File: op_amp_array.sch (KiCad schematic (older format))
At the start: 20 parts

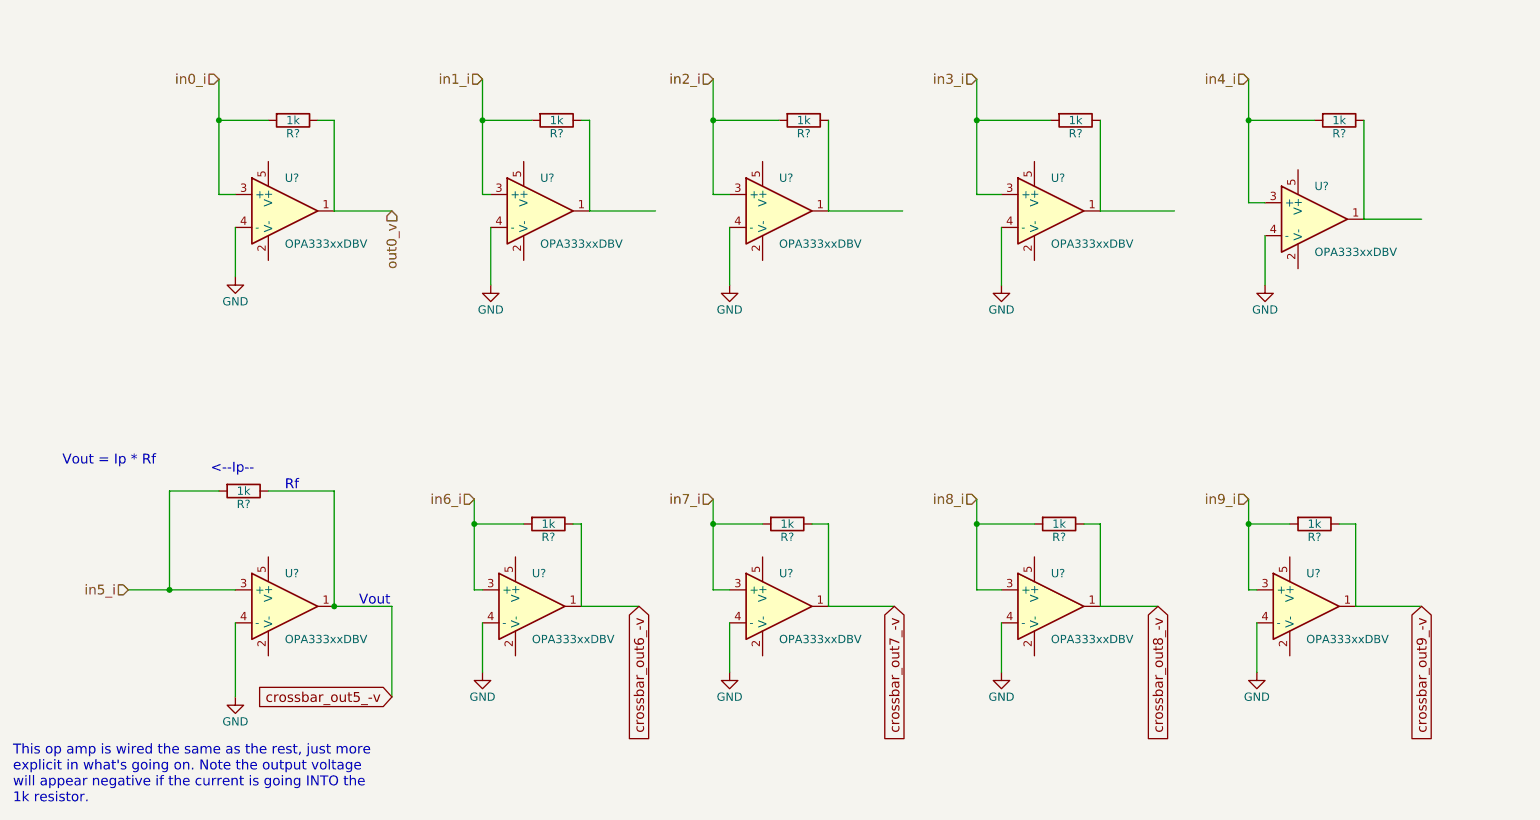
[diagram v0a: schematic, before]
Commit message: Additional Heirarchy Changes
Added resistor pages, still need to update values on them. See weight matrix file.
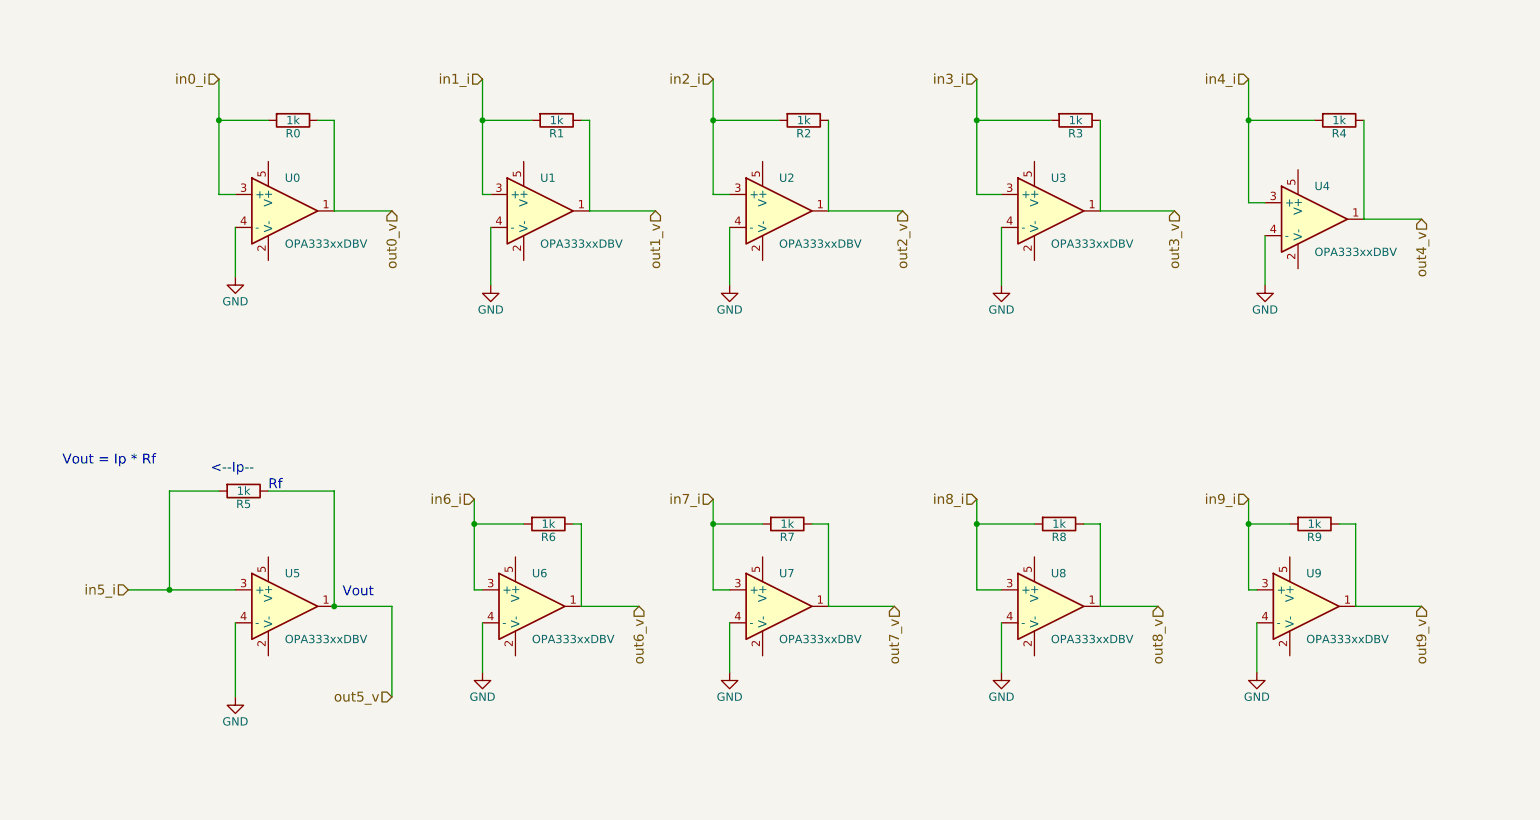
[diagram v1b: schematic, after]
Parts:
- gave numbers to parts that had none: 20
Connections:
- net labels added: out1_v, out2_v, out3_v, out4_v, out5_v, out6_v, out7_v, out8_v, out9_v
- net labels removed: crossbar_out5_-v, crossbar_out6_-v, crossbar_out7_-v, crossbar_out8_-v, crossbar_out9_-v
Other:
- note removed: "This op amp is wired the same as the rest, just more\nexplicit in what's going on. Note the output voltage \nwill appear negative if the current is going INTO the \n1k resistor."
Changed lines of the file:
@@
 $Descr A4 11693 8268
 encoding utf-8
-Sheet 2 3
-Title ""
+Sheet 2 7
+Title "Op Amp Array"
 Date ""
 Rev ""
-Comp ""
+Comp "Emulating NN with Resistor Network"
 Comment1 ""
 Comment2 ""
@@
 $EndDescr
 $Comp
-L OPA333xxDBV U?
+L OPA333xxDBV U4
 U 1 1 5C6B8B0D
 P 8800 2350
-F 0 "U?" H 8800 2550 50  0000 L CNN
+F 0 "U4" H 8800 2550 50  0000 L CNN
 F 1 "OPA333xxDBV" H 8800 2150 50  0000 L CNN
 F 2 "" H 8800 2350 50  0001 C CNN
@@
 $EndComp
 $Comp
-L OPA333xxDBV U?
+L OPA333xxDBV U5
 U 1 1 5C6B8B14
 P 2550 4700
-F 0 "U?" H 2550 4900 50  0000 L CNN
+F 0 "U5" H 2550 4900 50  0000 L CNN
 F 1 "OPA333xxDBV" H 2550 4500 50  0000 L CNN
 F 2 "" H 2550 4700 50  0001 C CNN
@@
 $EndComp
 $Comp
-L OPA333xxDBV U?
+L OPA333xxDBV U7
 U 1 1 5C6B8B1B
 P 5550 4700
-F 0 "U?" H 5550 4900 50  0000 L CNN
+F 0 "U7" H 5550 4900 50  0000 L CNN
 F 1 "OPA333xxDBV" H 5550 4500 50  0000 L CNN
 F 2 "" H 5550 4700 50  0001 C CNN
@@
 $EndComp
 $Comp
-L OPA333xxDBV U?
+L OPA333xxDBV U9
 U 1 1 5C6B8B22
 P 8750 4700
-F 0 "U?" H 8750 4900 50  0000 L CNN
+F 0 "U9" H 8750 4900 50  0000 L CNN
 F 1 "OPA333xxDBV" H 8750 4500 50  0000 L CNN
 F 2 "" H 8750 4700 50  0001 C CNN
@@
 $EndComp
 $Comp
-L OPA333xxDBV U?
+L OPA333xxDBV U2
 U 1 1 5C6B8B29
 P 5550 2300
-F 0 "U?" H 5550 2500 50  0000 L CNN
+F 0 "U2" H 5550 2500 50  0000 L CNN
 F 1 "OPA333xxDBV" H 5550 2100 50  0000 L CNN
 F 2 "" H 5550 2300 50  0001 C CNN
@@
 $EndComp
 $Comp
-L OPA333xxDBV U?
+L OPA333xxDBV U3
 U 1 1 5C6B8B30
 P 7200 2300
-F 0 "U?" H 7200 2500 50  0000 L CNN
+F 0 "U3" H 7200 2500 50  0000 L CNN
 F 1 "OPA333xxDBV" H 7200 2100 50  0000 L CNN
 F 2 "" H 7200 2300 50  0001 C CNN
@@
 $EndComp
 $Comp
-L OPA333xxDBV U?
+L OPA333xxDBV U6
 U 1 1 5C6B8B37
 P 4050 4700
-F 0 "U?" H 4050 4900 50  0000 L CNN
+F 0 "U6" H 4050 4900 50  0000 L CNN
 F 1 "OPA333xxDBV" H 4050 4500 50  0000 L CNN
 F 2 "" H 4050 4700 50  0001 C CNN
@@
 $EndComp
 $Comp
-L OPA333xxDBV U?
+L OPA333xxDBV U8
 U 1 1 5C6B8B3E
 P 7200 4700
-F 0 "U?" H 7200 4900 50  0000 L CNN
+F 0 "U8" H 7200 4900 50  0000 L CNN
 F 1 "OPA333xxDBV" H 7200 4500 50  0000 L CNN
 F 2 "" H 7200 4700 50  0001 C CNN
@@
 $EndComp
 $Comp
-L OPA333xxDBV U?
+L OPA333xxDBV U1
 U 1 1 5C6B8B45
 P 4100 2300
-F 0 "U?" H 4100 2500 50  0000 L CNN
+F 0 "U1" H 4100 2500 50  0000 L CNN
 F 1 "OPA333xxDBV" H 4100 2100 50  0000 L CNN
 F 2 "" H 4100 2300 50  0001 C CNN
@@
 $EndComp
 $Comp
-L OPA333xxDBV U?
+L OPA333xxDBV U0
 U 1 1 5C6B8B4C
 P 2550 2300
-F 0 "U?" H 2550 2500 50  0000 L CNN
+F 0 "U0" H 2550 2500 50  0000 L CNN
 F 1 "OPA333xxDBV" H 2550 2100 50  0000 L CNN
 F 2 "" H 2550 2300 50  0001 C CNN
@@
 	2250 4800 2250 5250
 $Comp
-L R R?
+L R R5
 U 1 1 5C6B8B54
 P 2300 4000
-F 0 "R?" V 2380 4000 50  0000 C CNN
+F 0 "R5" V 2380 4000 50  0000 C CNN
 F 1 "1k" V 2300 4000 50  0000 C CNN
 F 2 "" V 2230 4000 50  0001 C CNN
@@
 	3200 4700 3200 5250
 Connection ~ 2850 4700
-Text GLabel 3200 5250 0    60   Input ~ 0
-crossbar_out5_-v
 Text Notes 1200 3850 0    60   ~ 0
 Vout = Ip * Rf
-Text Notes 3000 4700 0    60   ~ 0
+Text Notes 2900 4650 0    60   ~ 0
 Vout
-Text Notes 2550 4000 0    60   ~ 0
+Text Notes 2450 4000 0    60   ~ 0
 Rf
 Text Notes 2100 3900 0    60   ~ 0
@@
 	8400 2250 8500 2250
 $Comp
-L R R?
+L R R0
 U 1 1 5C6B8B79
 P 2600 1750
-F 0 "R?" V 2680 1750 50  0000 C CNN
+F 0 "R0" V 2680 1750 50  0000 C CNN
 F 1 "1k" V 2600 1750 50  0000 C CNN
 F 2 "" V 2530 1750 50  0001 C CNN
@@
 $EndComp
 $Comp
-L R R?
+L R R1
 U 1 1 5C6B8B80
 P 4200 1750
-F 0 "R?" V 4280 1750 50  0000 C CNN
+F 0 "R1" V 4280 1750 50  0000 C CNN
 F 1 "1k" V 4200 1750 50  0000 C CNN
 F 2 "" V 4130 1750 50  0001 C CNN
@@
 $EndComp
 $Comp
-L R R?
+L R R2
 U 1 1 5C6B8B87
 P 5700 1750
-F 0 "R?" V 5780 1750 50  0000 C CNN
+F 0 "R2" V 5780 1750 50  0000 C CNN
 F 1 "1k" V 5700 1750 50  0000 C CNN
 F 2 "" V 5630 1750 50  0001 C CNN
@@
 $EndComp
 $Comp
-L R R?
+L R R3
 U 1 1 5C6B8B8E
 P 7350 1750
-F 0 "R?" V 7430 1750 50  0000 C CNN
+F 0 "R3" V 7430 1750 50  0000 C CNN
 F 1 "1k" V 7350 1750 50  0000 C CNN
 F 2 "" V 7280 1750 50  0001 C CNN
@@
 $EndComp
 $Comp
-L R R?
+L R R4
 U 1 1 5C6B8B95
 P 8950 1750
-F 0 "R?" V 9030 1750 50  0000 C CNN
+F 0 "R4" V 9030 1750 50  0000 C CNN
 F 1 "1k" V 8950 1750 50  0000 C CNN
 F 2 "" V 8880 1750 50  0001 C CNN
@@
 	8400 4600 8450 4600
 $Comp
-L R R?
+L R R8
 U 1 1 5C6B8BB5
 P 7250 4200
-F 0 "R?" V 7330 4200 50  0000 C CNN
+F 0 "R8" V 7330 4200 50  0000 C CNN
 F 1 "1k" V 7250 4200 50  0000 C CNN
 F 2 "" V 7180 4200 50  0001 C CNN
@@
 $EndComp
 $Comp
-L R R?
+L R R7
 U 1 1 5C6B8BBC
 P 5600 4200
-F 0 "R?" V 5680 4200 50  0000 C CNN
+F 0 "R7" V 5680 4200 50  0000 C CNN
 F 1 "1k" V 5600 4200 50  0000 C CNN
 F 2 "" V 5530 4200 50  0001 C CNN
@@
 $EndComp
 $Comp
-L R R?
+L R R6
 U 1 1 5C6B8BC3
 P 4150 4200
-F 0 "R?" V 4230 4200 50  0000 C CNN
+F 0 "R6" V 4230 4200 50  0000 C CNN
 F 1 "1k" V 4150 4200 50  0000 C CNN
 F 2 "" V 4080 4200 50  0001 C CNN
@@
 $EndComp
 $Comp
-L R R?
+L R R9
 U 1 1 5C6B8BCA
 P 8800 4200
-F 0 "R?" V 8880 4200 50  0000 C CNN
+F 0 "R9" V 8880 4200 50  0000 C CNN
 F 1 "1k" V 8800 4200 50  0000 C CNN
 F 2 "" V 8730 4200 50  0001 C CNN
@@
 Wire Wire Line
 	5850 4200 5850 4700
-Text Notes 900  5900 0    60   ~ 0
-This op amp is wired the same as the rest, just more\nexplicit in what's going on. Note the output voltage \nwill appear negative if the current is going INTO the \n1k resistor.
 $Comp
 L GND #PWR?
@@
 Wire Wire Line
 	3750 4800 3750 5100
-Text GLabel 4700 4700 3    60   Input ~ 0
-crossbar_out6_-v
-Text GLabel 6250 4700 3    60   Input ~ 0
-crossbar_out7_-v
-Text GLabel 7850 4700 3    60   Input ~ 0
-crossbar_out8_-v
-Text GLabel 9450 4700 3    60   Input ~ 0
-crossbar_out9_-v
 Wire Wire Line
 	9050 4700 9450 4700
@@
 Text HLabel 3200 2300 3    60   Input ~ 0
 out0_v
+Text HLabel 4800 2300 3    60   Input ~ 0
+out1_v
+Text HLabel 6300 2300 3    60   Input ~ 0
+out2_v
+Text HLabel 7950 2300 3    60   Input ~ 0
+out3_v
+Text HLabel 9450 2350 3    60   Input ~ 0
+out4_v
+Text HLabel 3200 5250 0    60   Input ~ 0
+out5_v
+Text HLabel 4700 4700 3    60   Input ~ 0
+out6_v
+Text HLabel 6250 4700 3    60   Input ~ 0
+out7_v
+Text HLabel 7850 4700 3    60   Input ~ 0
+out8_v
+Text HLabel 9450 4700 3    60   Input ~ 0
+out9_v
 $EndSCHEMATC

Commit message: Added footprints, finished schematic, began PCB layout
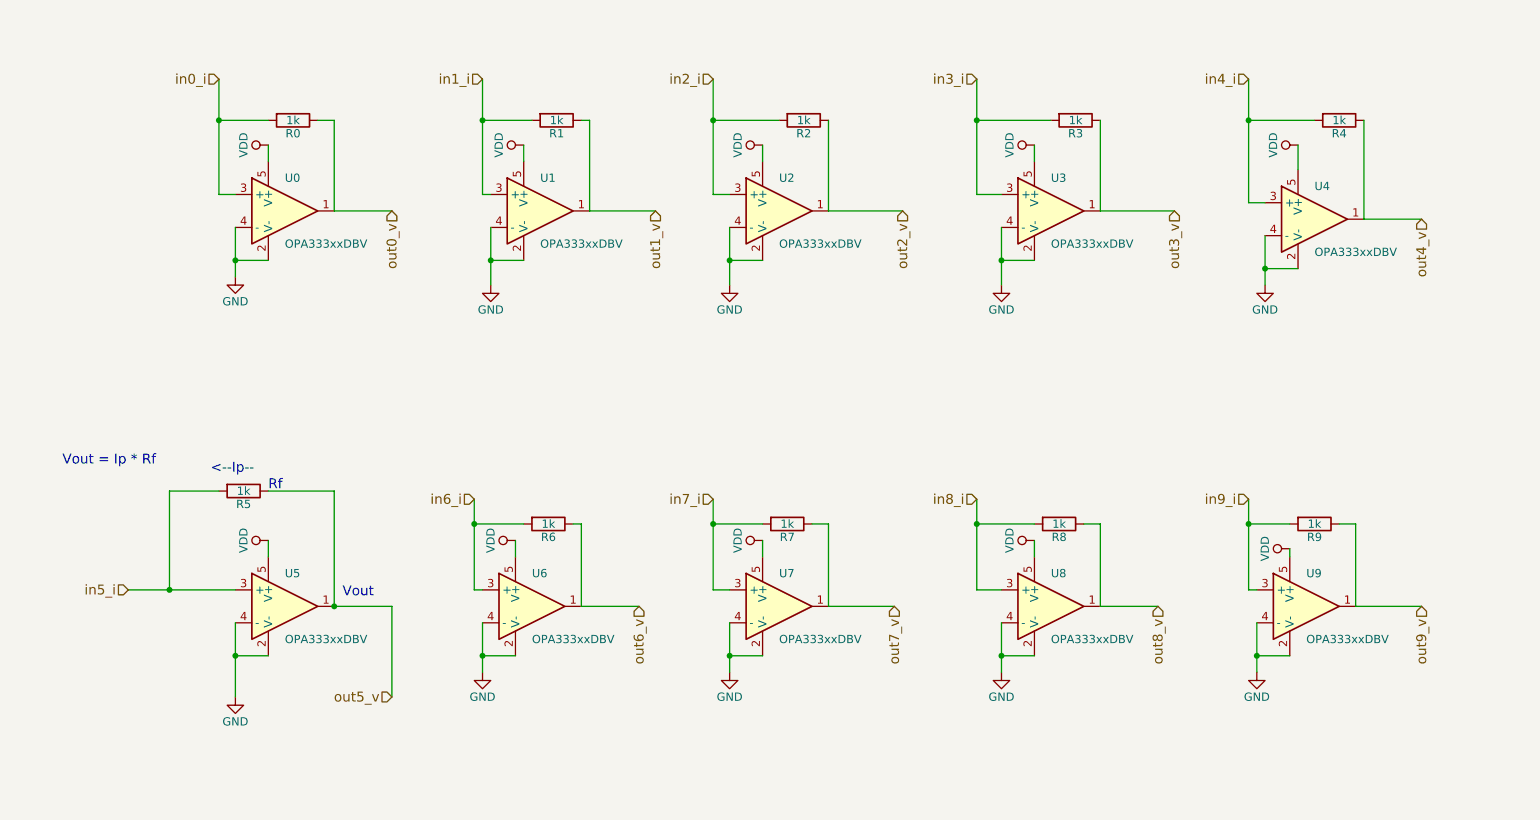
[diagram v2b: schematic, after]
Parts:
- R0, R1, R2, R3, R4, R5, R6, R7, R8, R9: footprint (none) -> Resistors_SMD:R_1206
- U0, U1, U2, U3, U4, U5, U6, U7, U8, U9: footprint (none) -> TO_SOT_Packages_SMD:SOT-23-5
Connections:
- net GND: now also U0.2 (V-), U1.2 (V-), U2.2 (V-), U3.2 (V-), U4.2 (V-), U5.2 (V-), U6.2 (V-), U7.2 (V-), U8.2 (V-), U9.2 (V-)
- net VDD: now reaches U4.5 (V+)
- net VDD: now also U0.5 (V+), U1.5 (V+), U2.5 (V+), U3.5 (V+), U5.5 (V+), U6.5 (V+), U7.5 (V+), U8.5 (V+), U9.5 (V+)

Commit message: fixed resistor schematic errors
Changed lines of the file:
@@
 	6900 5100 6900 4800
-Wire Wire Line
-	5250 5100 5250 4800
 Wire Wire Line
 	3750 4800 3750 5100
@@
 	7100 5000 6900 5000
 Connection ~ 6900 5000
-Wire Wire Line
-	5450 5000 5250 5000
 Connection ~ 5250 5000
 Wire Wire Line
@@
 	0    -1   -1   0
 $EndComp
+Wire Wire Line
+	5250 4800 5250 5100
+Wire Wire Line
+	5250 5000 5450 5000
 $EndSCHEMATC

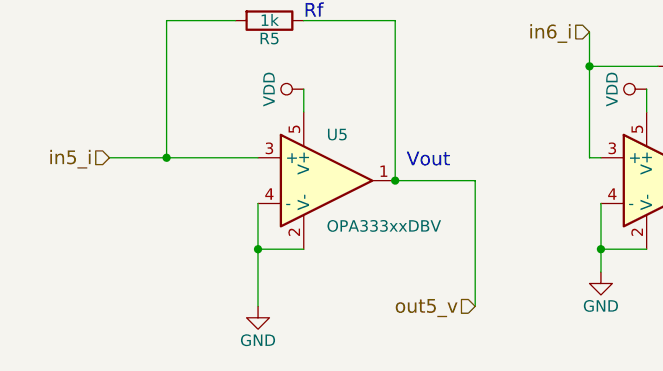
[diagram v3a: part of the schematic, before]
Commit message: fixed all ERC errors
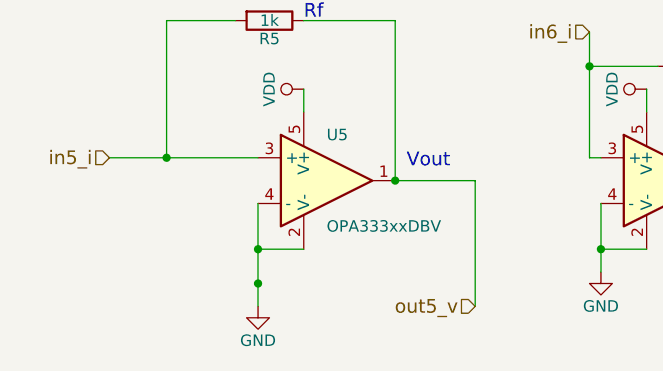
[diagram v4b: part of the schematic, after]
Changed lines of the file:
@@
 	6750 2200 6900 2200
 $Comp
-L GND #PWR03
+L GND #PWR05
 U 1 1 5C6B8B71
 P 2250 5250
-F 0 "#PWR03" H 2250 5000 50  0001 C CNN
+F 0 "#PWR05" H 2250 5000 50  0001 C CNN
 F 1 "GND" H 2250 5100 50  0000 C CNN
 F 2 "" H 2250 5250 50  0001 C CNN
@@
 	5850 4200 5850 4700
 $Comp
-L GND #PWR04
+L GND #PWR06
 U 1 1 5C6B8BE2
 P 3750 5100
-F 0 "#PWR04" H 3750 4850 50  0001 C CNN
+F 0 "#PWR06" H 3750 4850 50  0001 C CNN
 F 1 "GND" H 3750 4950 50  0000 C CNN
 F 2 "" H 3750 5100 50  0001 C CNN
@@
 $EndComp
 $Comp
-L GND #PWR05
+L GND #PWR07
 U 1 1 5C6B8BE8
 P 5250 5100
-F 0 "#PWR05" H 5250 4850 50  0001 C CNN
+F 0 "#PWR07" H 5250 4850 50  0001 C CNN
 F 1 "GND" H 5250 4950 50  0000 C CNN
 F 2 "" H 5250 5100 50  0001 C CNN
@@
 $EndComp
 $Comp
-L GND #PWR06
+L GND #PWR08
 U 1 1 5C6B8BEE
 P 6900 5100
-F 0 "#PWR06" H 6900 4850 50  0001 C CNN
+F 0 "#PWR08" H 6900 4850 50  0001 C CNN
 F 1 "GND" H 6900 4950 50  0000 C CNN
 F 2 "" H 6900 5100 50  0001 C CNN
@@
 $EndComp
 $Comp
-L GND #PWR07
+L GND #PWR09
 U 1 1 5C6B8BF4
 P 8450 5100
-F 0 "#PWR07" H 8450 4850 50  0001 C CNN
+F 0 "#PWR09" H 8450 4850 50  0001 C CNN
 F 1 "GND" H 8450 4950 50  0000 C CNN
 F 2 "" H 8450 5100 50  0001 C CNN
@@
 $EndComp
 $Comp
-L GND #PWR08
+L GND #PWR010
 U 1 1 5C6B8BFA
 P 2250 2700
-F 0 "#PWR08" H 2250 2450 50  0001 C CNN
+F 0 "#PWR010" H 2250 2450 50  0001 C CNN
 F 1 "GND" H 2250 2550 50  0000 C CNN
 F 2 "" H 2250 2700 50  0001 C CNN
@@
 $EndComp
 $Comp
-L GND #PWR09
+L GND #PWR011
 U 1 1 5C6B8C00
 P 3800 2750
-F 0 "#PWR09" H 3800 2500 50  0001 C CNN
+F 0 "#PWR011" H 3800 2500 50  0001 C CNN
 F 1 "GND" H 3800 2600 50  0000 C CNN
 F 2 "" H 3800 2750 50  0001 C CNN
@@
 $EndComp
 $Comp
-L GND #PWR010
+L GND #PWR012
 U 1 1 5C6B8C06
 P 5250 2750
-F 0 "#PWR010" H 5250 2500 50  0001 C CNN
+F 0 "#PWR012" H 5250 2500 50  0001 C CNN
 F 1 "GND" H 5250 2600 50  0000 C CNN
 F 2 "" H 5250 2750 50  0001 C CNN
@@
 $EndComp
 $Comp
-L GND #PWR011
+L GND #PWR013
 U 1 1 5C6B8C0C
 P 6900 2750
-F 0 "#PWR011" H 6900 2500 50  0001 C CNN
+F 0 "#PWR013" H 6900 2500 50  0001 C CNN
 F 1 "GND" H 6900 2600 50  0000 C CNN
 F 2 "" H 6900 2750 50  0001 C CNN
@@
 $EndComp
 $Comp
-L GND #PWR012
+L GND #PWR014
 U 1 1 5C6B8C12
 P 8500 2750
-F 0 "#PWR012" H 8500 2500 50  0001 C CNN
+F 0 "#PWR014" H 8500 2500 50  0001 C CNN
 F 1 "GND" H 8500 2600 50  0000 C CNN
 F 2 "" H 8500 2750 50  0001 C CNN
@@
 	4000 1900 4000 2000
 $Comp
-L VDD #PWR013
+L VDD #PWR015
 U 1 1 5C9CCA95
 P 2450 1900
-F 0 "#PWR013" H 2450 1750 50  0001 C CNN
+F 0 "#PWR015" H 2450 1750 50  0001 C CNN
 F 1 "VDD" H 2450 2050 50  0000 C CNN
 F 2 "" H 2450 1900 50  0001 C CNN
@@
 $EndComp
 $Comp
-L VDD #PWR014
+L VDD #PWR016
 U 1 1 5C9CCAE3
 P 4000 1900
-F 0 "#PWR014" H 4000 1750 50  0001 C CNN
+F 0 "#PWR016" H 4000 1750 50  0001 C CNN
 F 1 "VDD" H 4000 2050 50  0000 C CNN
 F 2 "" H 4000 1900 50  0001 C CNN
@@
 $EndComp
 $Comp
-L VDD #PWR015
+L VDD #PWR017
 U 1 1 5C9CCB2A
 P 5450 1900
-F 0 "#PWR015" H 5450 1750 50  0001 C CNN
+F 0 "#PWR017" H 5450 1750 50  0001 C CNN
 F 1 "VDD" H 5450 2050 50  0000 C CNN
 F 2 "" H 5450 1900 50  0001 C CNN
@@
 $EndComp
 $Comp
-L VDD #PWR016
+L VDD #PWR018
 U 1 1 5C9CCB71
 P 7100 1900
-F 0 "#PWR016" H 7100 1750 50  0001 C CNN
+F 0 "#PWR018" H 7100 1750 50  0001 C CNN
 F 1 "VDD" H 7100 2050 50  0000 C CNN
 F 2 "" H 7100 1900 50  0001 C CNN
@@
 $EndComp
 $Comp
-L VDD #PWR017
+L VDD #PWR019
 U 1 1 5C9CCBB8
 P 8700 1900
-F 0 "#PWR017" H 8700 1750 50  0001 C CNN
+F 0 "#PWR019" H 8700 1750 50  0001 C CNN
 F 1 "VDD" H 8700 2050 50  0000 C CNN
 F 2 "" H 8700 1900 50  0001 C CNN
@@
 $EndComp
 $Comp
-L VDD #PWR018
+L VDD #PWR020
 U 1 1 5C9CCBFF
 P 8650 4350
-F 0 "#PWR018" H 8650 4200 50  0001 C CNN
+F 0 "#PWR020" H 8650 4200 50  0001 C CNN
 F 1 "VDD" H 8650 4500 50  0000 C CNN
 F 2 "" H 8650 4350 50  0001 C CNN
@@
 $EndComp
 $Comp
-L VDD #PWR019
+L VDD #PWR021
 U 1 1 5C9CCC46
 P 7100 4300
-F 0 "#PWR019" H 7100 4150 50  0001 C CNN
+F 0 "#PWR021" H 7100 4150 50  0001 C CNN
 F 1 "VDD" H 7100 4450 50  0000 C CNN
 F 2 "" H 7100 4300 50  0001 C CNN
@@
 $EndComp
 $Comp
-L VDD #PWR020
+L VDD #PWR022
 U 1 1 5C9CCC8D
 P 5450 4300
-F 0 "#PWR020" H 5450 4150 50  0001 C CNN
+F 0 "#PWR022" H 5450 4150 50  0001 C CNN
 F 1 "VDD" H 5450 4450 50  0000 C CNN
 F 2 "" H 5450 4300 50  0001 C CNN
@@
 $EndComp
 $Comp
-L VDD #PWR021
+L VDD #PWR023
 U 1 1 5C9CCCD4
 P 3950 4300
-F 0 "#PWR021" H 3950 4150 50  0001 C CNN
+F 0 "#PWR023" H 3950 4150 50  0001 C CNN
 F 1 "VDD" H 3950 4450 50  0000 C CNN
 F 2 "" H 3950 4300 50  0001 C CNN
@@
 $EndComp
 $Comp
-L VDD #PWR022
+L VDD #PWR024
 U 1 1 5C9CCD1B
 P 2450 4300
-F 0 "#PWR022" H 2450 4150 50  0001 C CNN
+F 0 "#PWR024" H 2450 4150 50  0001 C CNN
 F 1 "VDD" H 2450 4450 50  0000 C CNN
 F 2 "" H 2450 4300 50  0001 C CNN
@@
 Wire Wire Line
 	5250 5000 5450 5000
+Connection ~ 2250 5150
 $EndSCHEMATC

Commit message: Circuit complete
Committing before I read in netlist just in case things get screwed
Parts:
- added R01, R02, R10, R11, R20, R21, R30, R31, R40, R41, R50, R51, R60, R61, R70, R71, R80, R81, R90, R91: 1k, Resistors_SMD:R_1206, symbol R
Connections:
- net VDD: now also R02.2, R11.2, R21.2, R31.2, R41.2, R51.2, R61.2, R71.2, R81.2, R91.2
- net out0_v: now also R01.2, R02.1; no longer R0.1, U0.1
- net out1_v: now also R10.2, R11.1; no longer R1.1, U1.1
- net out2_v: now also R20.2, R21.1; no longer R2.1, U2.1
- net out3_v: now also R30.2, R31.1; no longer R3.1, U3.1
- net out4_v: now also R40.2, R41.1; no longer R4.1, U4.1
- net out5_v: now also R50.2, R51.1; no longer R5.1, U5.1
- net out6_v: now also R60.2, R61.1; no longer R6.1, U6.1
- net out7_v: now also R70.2, R71.1; no longer R7.1, U7.1
- net out8_v: now also R80.2, R81.1; no longer R8.1, U8.1
- net out9_v: now also R90.2, R91.1; no longer R9.1, U9.1
- new net: R4.1, R40.1, U4.1
- new net: R5.1, R50.1, U5.1
- new net: R7.1, R70.1, U7.1
- new net: R9.1, R90.1, U9.1
- new net: R2.1, R20.1, U2.1
- new net: R3.1, R30.1, U3.1
- new net: R6.1, R60.1, U6.1
- new net: R8.1, R80.1, U8.1
- new net: R1.1, R10.1, U1.1
- new net: R0.1, R01.1, U0.1
